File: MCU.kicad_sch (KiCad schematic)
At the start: 7 parts, among them U2 ESP32-S3-WROOM-1-N32R16V

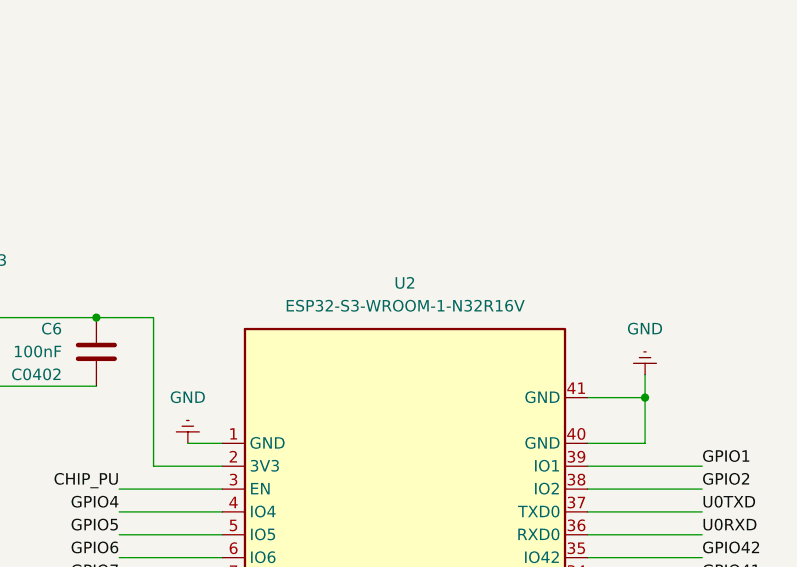
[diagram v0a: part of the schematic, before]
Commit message: done interfacePage
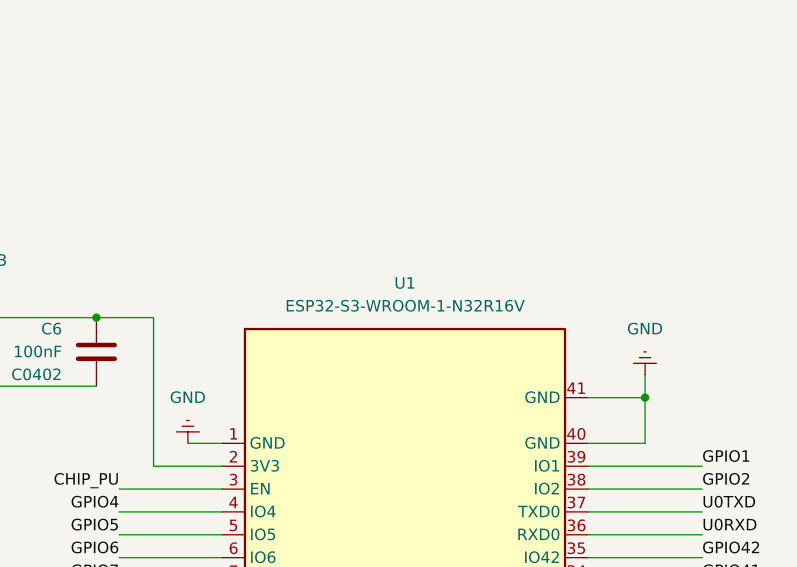
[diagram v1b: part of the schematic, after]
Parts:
- renumbered U2 to U1
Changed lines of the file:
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@@
 		(dnp no)
 		(fields_autoplaced yes)
-		(property "Reference" "U2"
+		(property "Reference" "U1"
 			(at 153.67 49.53 0)
 			(effects
@@
 			(project "EchoEarCopyProj"
 				(path "/cbd96126-2c6b-41c3-991f-657fa8ab5ecf/744180c9-1053-4012-ae45-7456444db5f3"
-					(reference "U2")
+					(reference "U1")
 					(unit 1)
 				)
